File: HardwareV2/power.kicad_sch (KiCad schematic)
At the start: 15 parts, among them CN1 S2B-PH-SM4-TB(LF)(SN), SW1 SW_SPDT, U2 BQ24040DSQR, U3 TPS63021DSJR

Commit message: commiting before flight :), added in crystal and started doing the labels for the RP2350b
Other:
- note added: "Feature: SW1 to allow user to turn the device on and off EN=1 device is enabled, EN=0 device is disabled"
- note removed: "Feature: SW1 to allow user to turn the device on and off"
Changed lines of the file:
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@@
 		)
 	)
-	(text "Feature: SW1 to allow user to turn the device on and off"
+	(text "Feature: SW1 to allow user to turn the device on and off\nEN=1 device is enabled, EN=0 device is disabled"
 		(exclude_from_sim no)
 		(at 160.528 93.472 0)

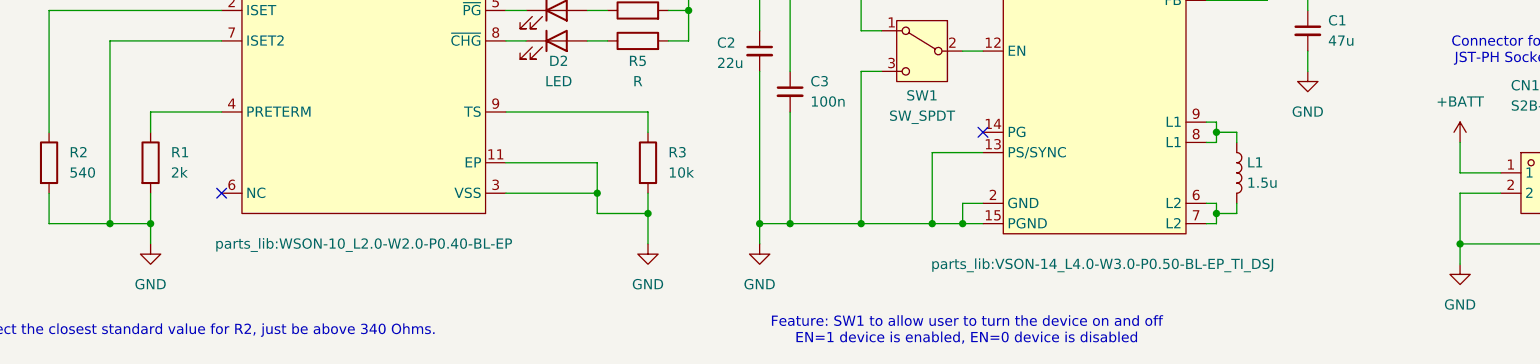
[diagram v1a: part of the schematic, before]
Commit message: initial v2 pcb layout minus passives
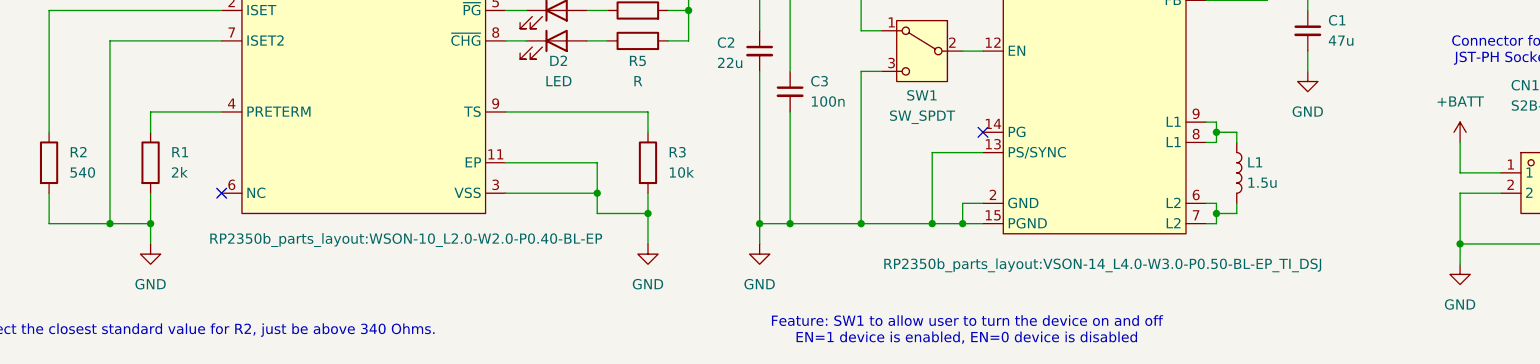
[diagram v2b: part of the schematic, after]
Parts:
- C1, C2, C3: footprint (none) -> Capacitor_SMD:C_0805_2012Metric
- CN1: footprint parts_lib:CONN-SMD_P2.00_S2B-PH-SM4-TB-LF-SN -> RP2350b_parts_layout:CONN-SMD_P2.00_S2B-PH-SM4-TB-LF-SN
- L1: footprint (none) -> Inductor_SMD:L_Coilcraft_XxL4020
- R1, R2, R3, R4, R5: footprint (none) -> Resistor_SMD:R_0805_2012Metric
- U2: footprint parts_lib:WSON-10_L2.0-W2.0-P0.40-BL-EP -> RP2350b_parts_layout:WSON-10_L2.0-W2.0-P0.40-BL-EP
- U3: footprint parts_lib:VSON-14_L4.0-W3.0-P0.50-BL-EP_TI_DSJ -> RP2350b_parts_layout:VSON-14_L4.0-W3.0-P0.50-BL-EP_TI_DSJ
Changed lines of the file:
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@@
 			)
 		)
-		(property "Footprint" ""
+		(property "Footprint" "Resistor_SMD:R_0805_2012Metric"
 			(at 119.38 55.118 90)
 			(effects
@@
 			)
 		)
-		(property "Footprint" ""
+		(property "Footprint" "Resistor_SMD:R_0805_2012Metric"
 			(at 119.38 58.928 90)
 			(effects
@@
 			)
 		)
-		(property "Footprint" ""
+		(property "Footprint" "Capacitor_SMD:C_0805_2012Metric"
 			(at 134.62 58.42 0)
 			(effects
@@
 			)
 		)
-		(property "Footprint" ""
+		(property "Footprint" "Resistor_SMD:R_0805_2012Metric"
 			(at 43.942 72.39 90)
 			(effects
@@
 			)
 		)
-		(property "Footprint" "parts_lib:VSON-14_L4.0-W3.0-P0.50-BL-EP_TI_DSJ"
+		(property "Footprint" "RP2350b_parts_layout:VSON-14_L4.0-W3.0-P0.50-BL-EP_TI_DSJ"
 			(at 177.546 85.09 0)
 			(effects
@@
 			)
 		)
-		(property "Footprint" ""
+		(property "Footprint" "Capacitor_SMD:C_0805_2012Metric"
 			(at 203.2 55.88 0)
 			(effects
@@
 			)
 		)
-		(property "Footprint" "parts_lib:CONN-SMD_P2.00_S2B-PH-SM4-TB-LF-SN"
+		(property "Footprint" "RP2350b_parts_layout:CONN-SMD_P2.00_S2B-PH-SM4-TB-LF-SN"
 			(at 231.14 88.9 0)
 			(effects
@@
 			)
 		)
-		(property "Footprint" ""
+		(property "Footprint" "Capacitor_SMD:C_0805_2012Metric"
 			(at 138.43 63.5 0)
 			(effects
@@
 			)
 		)
-		(property "Footprint" ""
+		(property "Footprint" "Inductor_SMD:L_Coilcraft_XxL4020"
 			(at 194.31 73.66 0)
 			(effects
@@
 		(on_board yes)
 		(dnp no)
-		(fields_autoplaced yes)
 		(property "Reference" "U2"
 			(at 85.09 39.37 0)
@@
 			)
 		)
-		(property "Footprint" "parts_lib:WSON-10_L2.0-W2.0-P0.40-BL-EP"
-			(at 85.09 82.55 0)
+		(property "Footprint" "RP2350b_parts_layout:WSON-10_L2.0-W2.0-P0.40-BL-EP"
+			(at 90.3453 81.9296 0)
 			(effects
 				(font
@@
 			)
 		)
-		(property "Footprint" ""
+		(property "Footprint" "Resistor_SMD:R_0805_2012Metric"
 			(at 118.872 72.39 90)
 			(effects
@@
 			)
 		)
-		(property "Footprint" ""
+		(property "Footprint" "Resistor_SMD:R_0805_2012Metric"
 			(at 56.642 72.39 90)
 			(effects
